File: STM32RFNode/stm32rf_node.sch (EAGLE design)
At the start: 6 parts

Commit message: rounting step 1
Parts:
- U$2: value NRF24L01+REFDESIGN -> NRF24L01+REFDESIGNMINI; device nRF24L01+RefDesign:NRF24L01+REFDESIGN -> nRF24L01+RefDesign:NRF24L01+REFDESIGNMINI
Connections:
- new net INT: U$1.PB_0, U$4.INT
- new net N$11: U$1.PC_15, U$2.CE
- net N$1: now also U$1.PA_7, U$2.MOSI; no longer U$1.PB_14, U$2.MISO
- net N$2: now also U$1.PA_6, U$2.MISO; no longer U$1.PB_15, U$2.MOSI
- net N$3: now also U$1.PA_5; no longer U$1.PB_13
- net N$4: now also U$1.PA_4; no longer U$1.PB_12
- net N$5: now also U$1.PB_1, U$4.A0; no longer U$1.PA_8, U$2.CE
- net N$6: now also U$1.PA_0; no longer U$1.PA_9

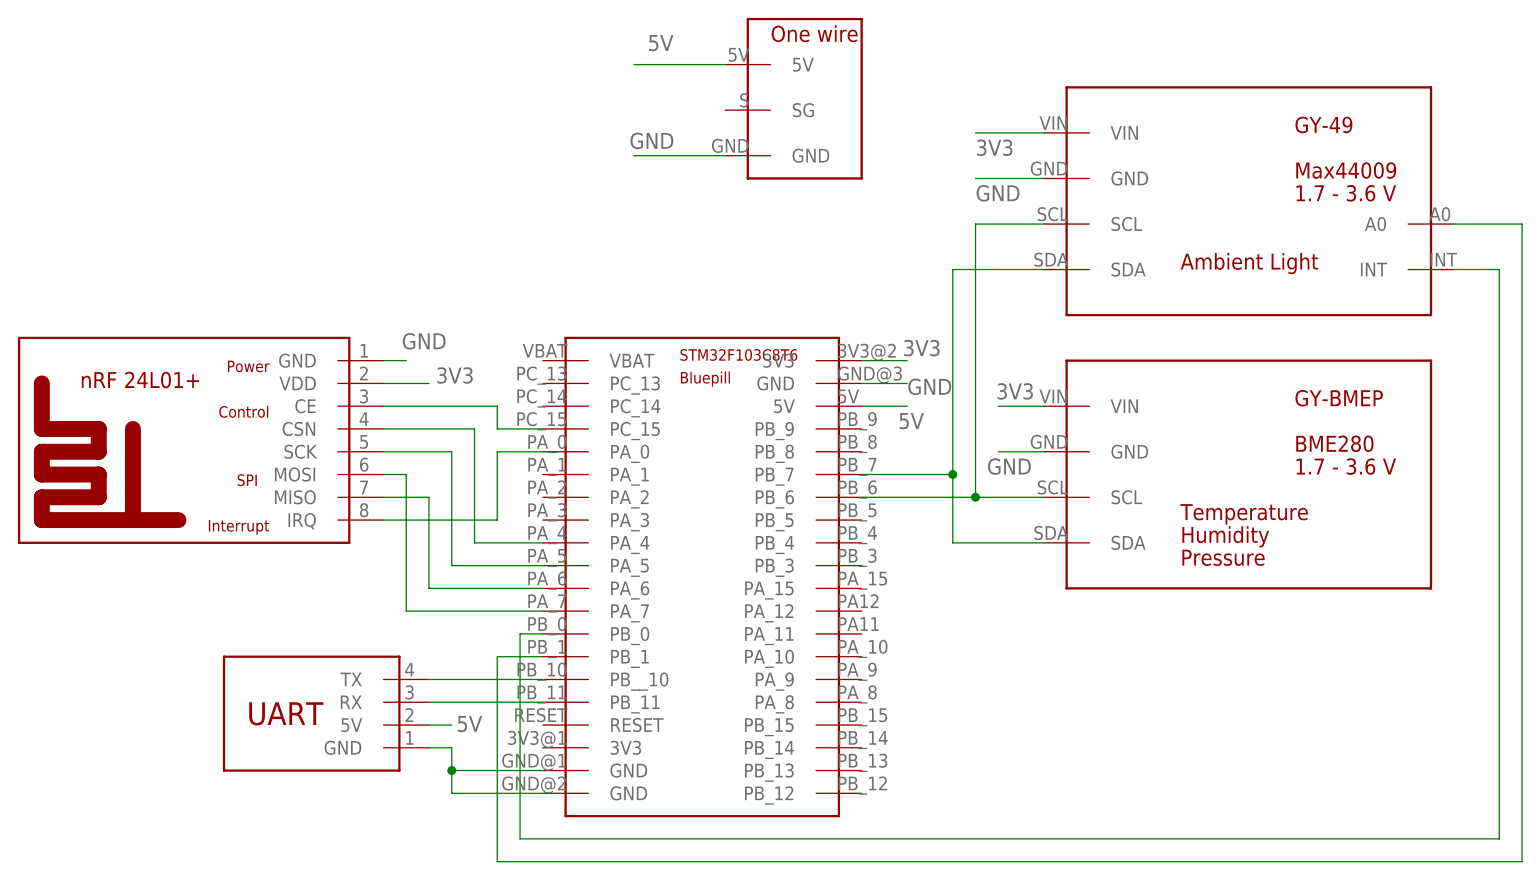
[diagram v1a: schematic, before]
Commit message: done routing with gnd rastnet
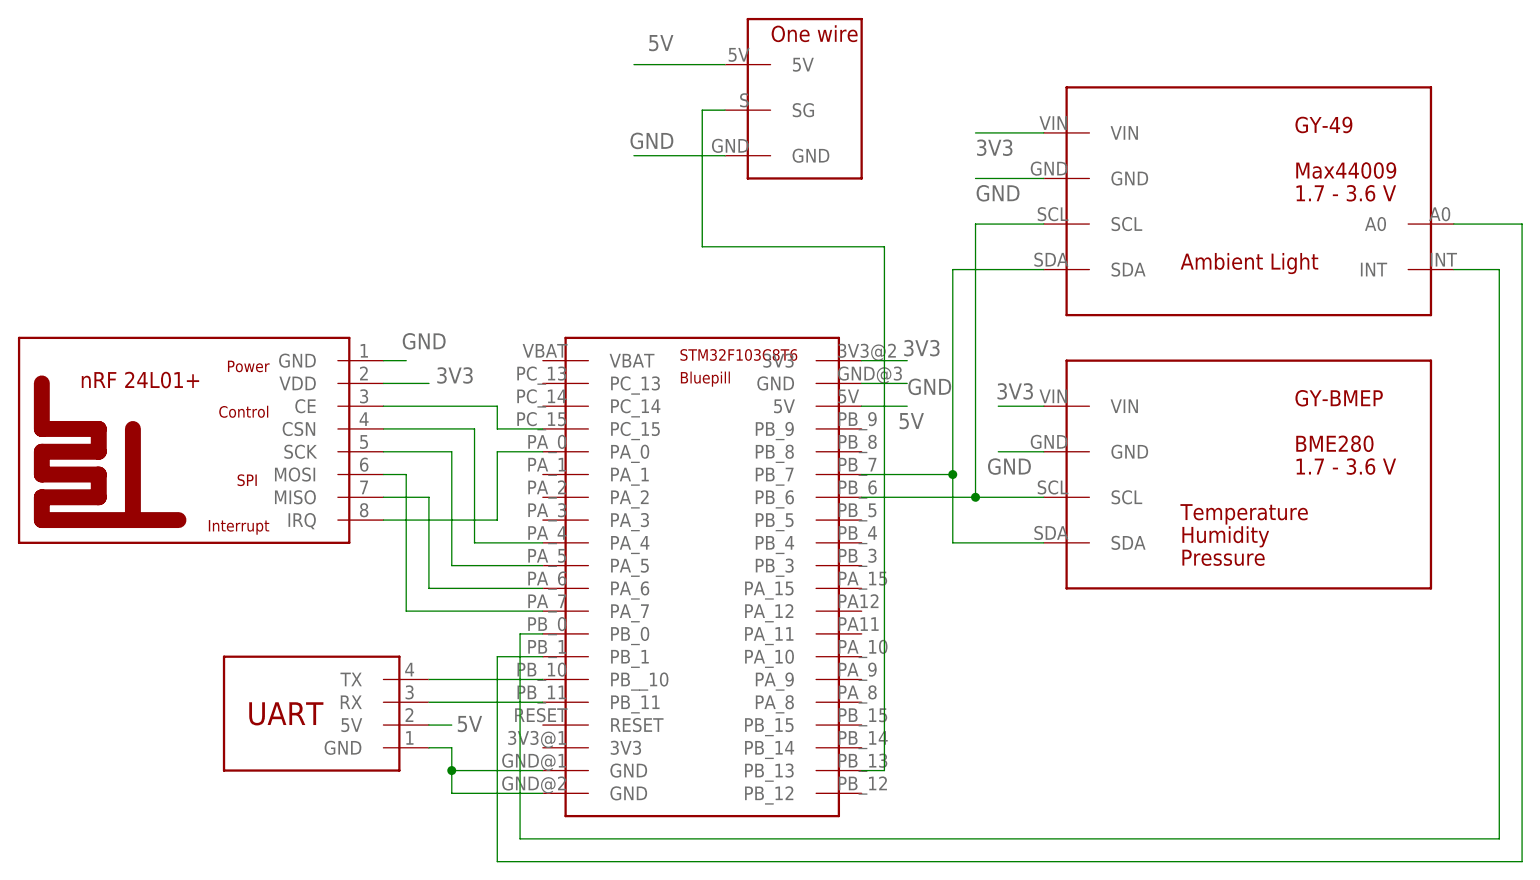
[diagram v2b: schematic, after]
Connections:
- new net N$12: U$1.PB_13, U$5.SG
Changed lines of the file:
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@@
+</segment>
+</net>
+<net name="N$12" class="0">
+<segment>
+<pinref part="U$1" gate="G$1" pin="PB_13"/>
+<wire x1="17.78" y1="-22.86" x2="20.32" y2="-22.86" width="0.1524" layer="91"/>
+<wire x1="20.32" y1="-22.86" x2="20.32" y2="35.56" width="0.1524" layer="91"/>
+<wire x1="20.32" y1="35.56" x2="0" y2="35.56" width="0.1524" layer="91"/>
+<wire x1="0" y1="35.56" x2="0" y2="50.8" width="0.1524" layer="91"/>
+<pinref part="U$5" gate="G$1" pin="SG"/>
+<wire x1="0" y1="50.8" x2="2.54" y2="50.8" width="0.1524" layer="91"/>
 </segment>
 </net>

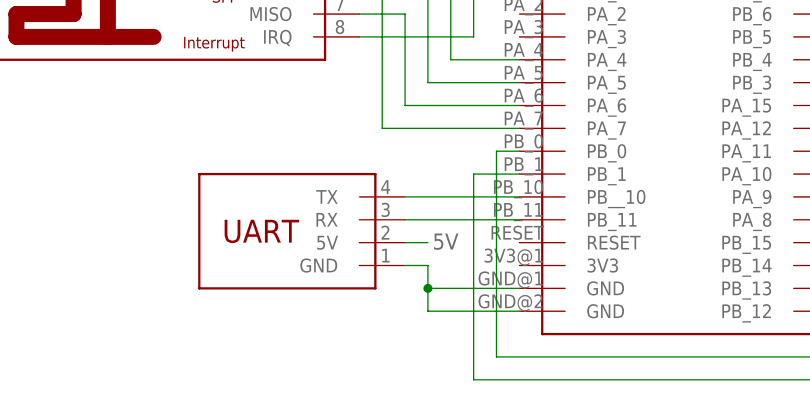
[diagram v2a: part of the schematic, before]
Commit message: Added possibility to connect the MPU 6050 on the I2C by shifting connections to match Add with Gnd
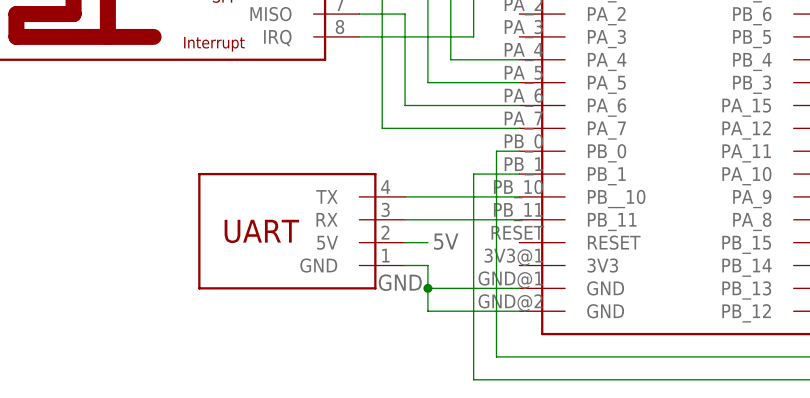
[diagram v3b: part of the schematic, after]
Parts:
- U$5: value ONE_WIRE -> ONE_WIRE'RIGHT'; device one-wire:ONE_WIRE -> one-wire:ONE_WIRE'RIGHT'
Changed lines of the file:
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@@
 <grid distance="0.1" unitdist="inch" unit="inch" style="lines" multiple="1" display="no" altdistance="0.01" altunitdist="inch" altunit="inch"/>
 <layers>
-<layer number="1" name="Top" color="4" fill="1" visible="no" active="no"/>
-<layer number="16" name="Bottom" color="1" fill="1" visible="no" active="no"/>
-<layer number="17" name="Pads" color="2" fill="1" visible="no" active="no"/>
-<layer number="18" name="Vias" color="2" fill="1" visible="no" active="no"/>
-<layer number="19" name="Unrouted" color="6" fill="1" visible="no" active="no"/>
-<layer number="20" name="Dimension" color="15" fill="1" visible="no" active="no"/>
-<layer number="21" name="tPlace" color="7" fill="1" visible="no" active="no"/>
-<layer number="22" name="bPlace" color="7" fill="1" visible="no" active="no"/>
-<layer number="23" name="tOrigins" color="15" fill="1" visible="no" active="no"/>
-<layer number="24" name="bOrigins" color="15" fill="1" visible="no" active="no"/>
-<layer number="25" name="tNames" color="7" fill="1" visible="no" active="no"/>
-<layer number="26" name="bNames" color="7" fill="1" visible="no" active="no"/>
-<layer number="27" name="tValues" color="7" fill="1" visible="no" active="no"/>
-<layer number="28" name="bValues" color="7" fill="1" visible="no" active="no"/>
+<layer number="1" name="Top" color="4" fill="1" visible="yes" active="no"/>
+<layer number="16" name="Bottom" color="1" fill="1" visible="yes" active="no"/>
+<layer number="17" name="Pads" color="2" fill="1" visible="yes" active="no"/>
+<layer number="18" name="Vias" color="2" fill="1" visible="yes" active="no"/>
+<layer number="19" name="Unrouted" color="6" fill="1" visible="yes" active="no"/>
+<layer number="20" name="Dimension" color="15" fill="1" visible="yes" active="no"/>
+<layer number="21" name="tPlace" color="7" fill="1" visible="yes" active="no"/>
+<layer number="22" name="bPlace" color="7" fill="1" visible="yes" active="no"/>
+<layer number="23" name="tOrigins" color="15" fill="1" visible="yes" active="no"/>
+<layer number="24" name="bOrigins" color="15" fill="1" visible="yes" active="no"/>
+<layer number="25" name="tNames" color="7" fill="1" visible="yes" active="no"/>
+<layer number="26" name="bNames" color="7" fill="1" visible="yes" active="no"/>
+<layer number="27" name="tValues" color="7" fill="1" visible="yes" active="no"/>
+<layer number="28" name="bValues" color="7" fill="1" visible="yes" active="no"/>
 <layer number="29" name="tStop" color="7" fill="3" visible="no" active="no"/>
 <layer number="30" name="bStop" color="7" fill="6" visible="no" active="no"/>
@@
 <layer number="35" name="tGlue" color="7" fill="4" visible="no" active="no"/>
 <layer number="36" name="bGlue" color="7" fill="5" visible="no" active="no"/>
-<layer number="37" name="tTest" color="7" fill="1" visible="no" active="no"/>
-<layer number="38" name="bTest" color="7" fill="1" visible="no" active="no"/>
+<layer number="37" name="tTest" color="7" fill="1" visible="yes" active="no"/>
+<layer number="38" name="bTest" color="7" fill="1" visible="yes" active="no"/>
 <layer number="39" name="tKeepout" color="4" fill="11" visible="no" active="no"/>
 <layer number="40" name="bKeepout" color="1" fill="11" visible="no" active="no"/>
@@
 <layer number="44" name="Drills" color="7" fill="1" visible="no" active="no"/>
 <layer number="45" name="Holes" color="7" fill="1" visible="no" active="no"/>
-<layer number="46" name="Milling" color="3" fill="1" visible="no" active="no"/>
-<layer number="47" name="Measures" color="7" fill="1" visible="no" active="no"/>
-<layer number="48" name="Document" color="7" fill="1" visible="no" active="no"/>
-<layer number="49" name="Reference" color="7" fill="1" visible="no" active="no"/>
-<layer number="51" name="tDocu" color="7" fill="1" visible="no" active="no"/>
-<layer number="52" name="bDocu" color="7" fill="1" visible="no" active="no"/>
+<layer number="46" name="Milling" color="3" fill="1" visible="yes" active="no"/>
+<layer number="47" name="Measures" color="7" fill="1" visible="yes" active="no"/>
+<layer number="48" name="Document" color="7" fill="1" visible="yes" active="no"/>
+<layer number="49" name="Reference" color="7" fill="1" visible="yes" active="no"/>
+<layer number="51" name="tDocu" color="7" fill="1" visible="yes" active="no"/>
+<layer number="52" name="bDocu" color="7" fill="1" visible="yes" active="no"/>
 <layer number="90" name="Modules" color="5" fill="1" visible="yes" active="yes"/>
 <layer number="91" name="Nets" color="2" fill="1" visible="yes" active="yes"/>
@@
 <part name="U$3" library="GY-BMEP" deviceset="GY-BMEP" device="GY-BMEP-NOHOLE" value="GY-BMEPGY-BMEP-NOHOLE"/>
 <part name="U$4" library="GY-49" deviceset="GY-49" device="G-49-SURF"/>
-<part name="U$5" library="one-wire" deviceset="ONE_WIRE" device=""/>
+<part name="U$5" library="one-wire" deviceset="ONE_WIRE" device="'RIGHT'" value="ONE_WIRE'RIGHT'"/>
 <part name="U$6" library="WFConnectors" deviceset="UART" device="MINI"/>
 </parts>
@@
 <wire x1="-17.78" y1="-22.86" x2="-27.94" y2="-22.86" width="0.1524" layer="91"/>
 <junction x="-27.94" y="-22.86"/>
+<label x="-33.528" y="-23.114" size="1.778" layer="95"/>
 </segment>
 <segment>

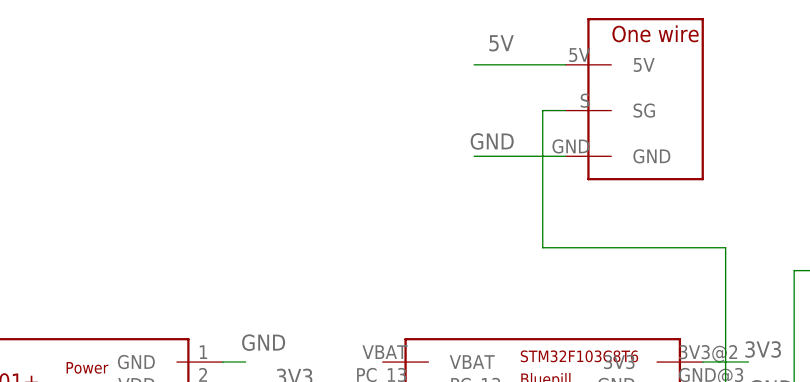
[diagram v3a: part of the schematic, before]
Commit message: new production with usb connector
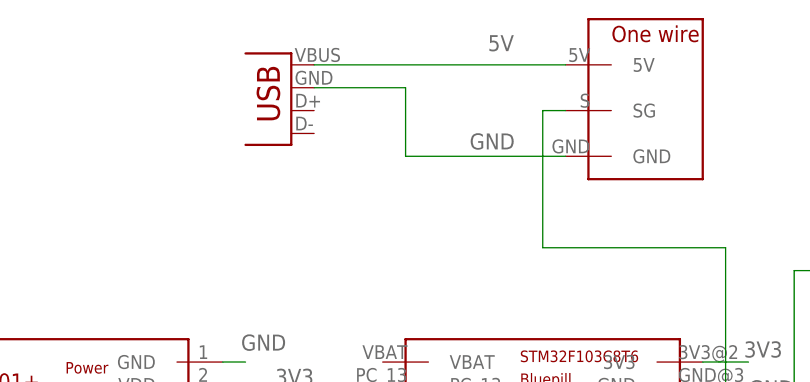
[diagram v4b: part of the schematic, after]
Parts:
- added X1: USB-A-H, usb:USB-A-H
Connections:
- net 5V: now also X1.GND
- net GND: now also X1.VBUS
